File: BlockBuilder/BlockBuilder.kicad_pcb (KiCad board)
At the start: 4 copper layers, 1 x 55.8 mm, 82 parts, among them J1 ARJM11C7-114-BA-EW2, T1 FA2924-AL, U1 W5500, U2 Si3402-B-GMR, U3 VO618A-3X017T, U4 TLV431BCDBZR, Y1 25.000MHz CL=12pF

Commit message: Finish the layout blocks: placement tests pass, docs updated
All nine fragments passed the BlockBuilder placement test on 2026-09-25:
footprints, segments, vias, zones and F.Fab labels arrived, and copper
matched each module board net by net. BlockBuilder keeps the PoE retest.

Per-footprint zone-connection overrides do not travel with a fragment. The
Buck, PowerMux and USBC Host-Setup pages say how to set the power pads to
solid in the host.

The PoE module gets its review-fix record (Layout-Spec section 17) and the new
line-side rule in Host-Setup. TODO.md closes the layout block list and lists
the fab questions and known limits. ARCHITECTURE.md carries the new
placement measurement.

Co-Authored-By: Claude Opus 5.5 (1M context) <noreply@anthropic.com>
Claude-Session: https://claude.ai/code/session_01ErAAfkmF4h3T5yfrw21utF
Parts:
- moved C10 62.9 mm to (44.0, 32.0)
- moved C12 62.9 mm to (44.0, 34.3)
- moved C14 62.9 mm to (38.0, 37.7)
- moved C15 62.9 mm to (60.5, 44.0)
- moved C17 62.9 mm to (44.0, 36.5)
- moved C18 62.9 mm to (49.2, 44.0)
- moved C21 62.9 mm to (49.2, 47.0)
- moved C22 62.9 mm to (53.0, 47.5)
- moved C24 62.9 mm to (35.0, 52.0)
- moved C25 62.9 mm to (47.0, 29.5)
- moved C26 62.9 mm to (47.0, 23.0)
- moved C27 62.9 mm to (44.5, 41.5)
- moved C28 62.9 mm to (54.0, 24.0)
- moved C30 62.9 mm to (36.2, 46.0)
- moved C33 62.9 mm to (44.5, 39.5)
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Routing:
- net /VPOS: track 5.15 -> 8.93 mm
- net GND: track 3.49 -> 7.03 mm, vias 11 -> 55
- net /MDI_RDP: track 23.0 -> 23.8 mm
- net /RCT: track 27.2 -> 27.9 mm
- net /XO: track 11.4 -> 10.8 mm
- net /MDI_RDN: track 19.4 -> 19.9 mm

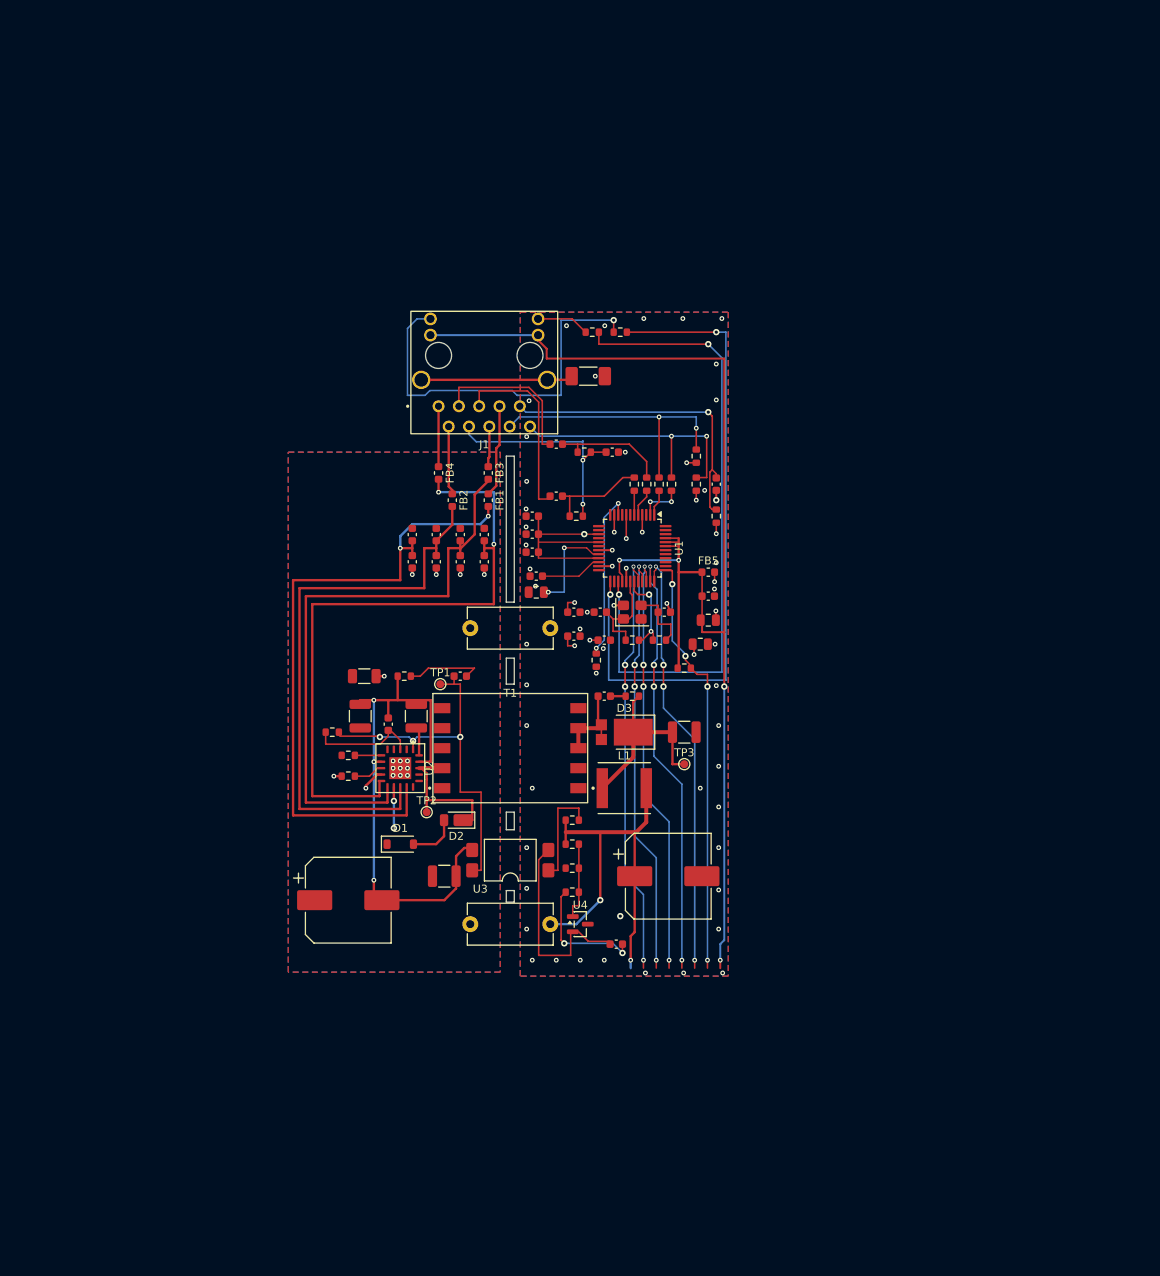
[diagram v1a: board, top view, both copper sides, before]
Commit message: Put the PoE block schematic on one A3 page
The block schematic spanned 296 mm on an A4 landscape page, and 37 of its 82
parts sat above the frame, so a print lost them.

- Two sheets inside one block do not work: KiCad 10.0.6 refuses to save a
  design block with a nested sheet. Tested on a scratch project.
- The sheet is now A3 portrait with every part inside the frame. Net
  membership is identical to before the move, ERC and DRC are unchanged, and
  the fragment's schematic is updated.
- Placed with Place as sheet, the block lands as its own A3 page with its
  title block. The full layout arrives, copper equal net by net.

Place as sheet prefixes every net with the sheet path, so /NAME net class
patterns bind nothing. Every Host-Setup.md now has section 5.3: use */NAME,
which binds the same nets on a flat placement.

BlockBuilder keeps this test.

Co-Authored-By: Claude Opus 5.5 (1M context) <noreply@anthropic.com>
Claude-Session: https://claude.ai/code/session_01ErAAfkmF4h3T5yfrw21utF
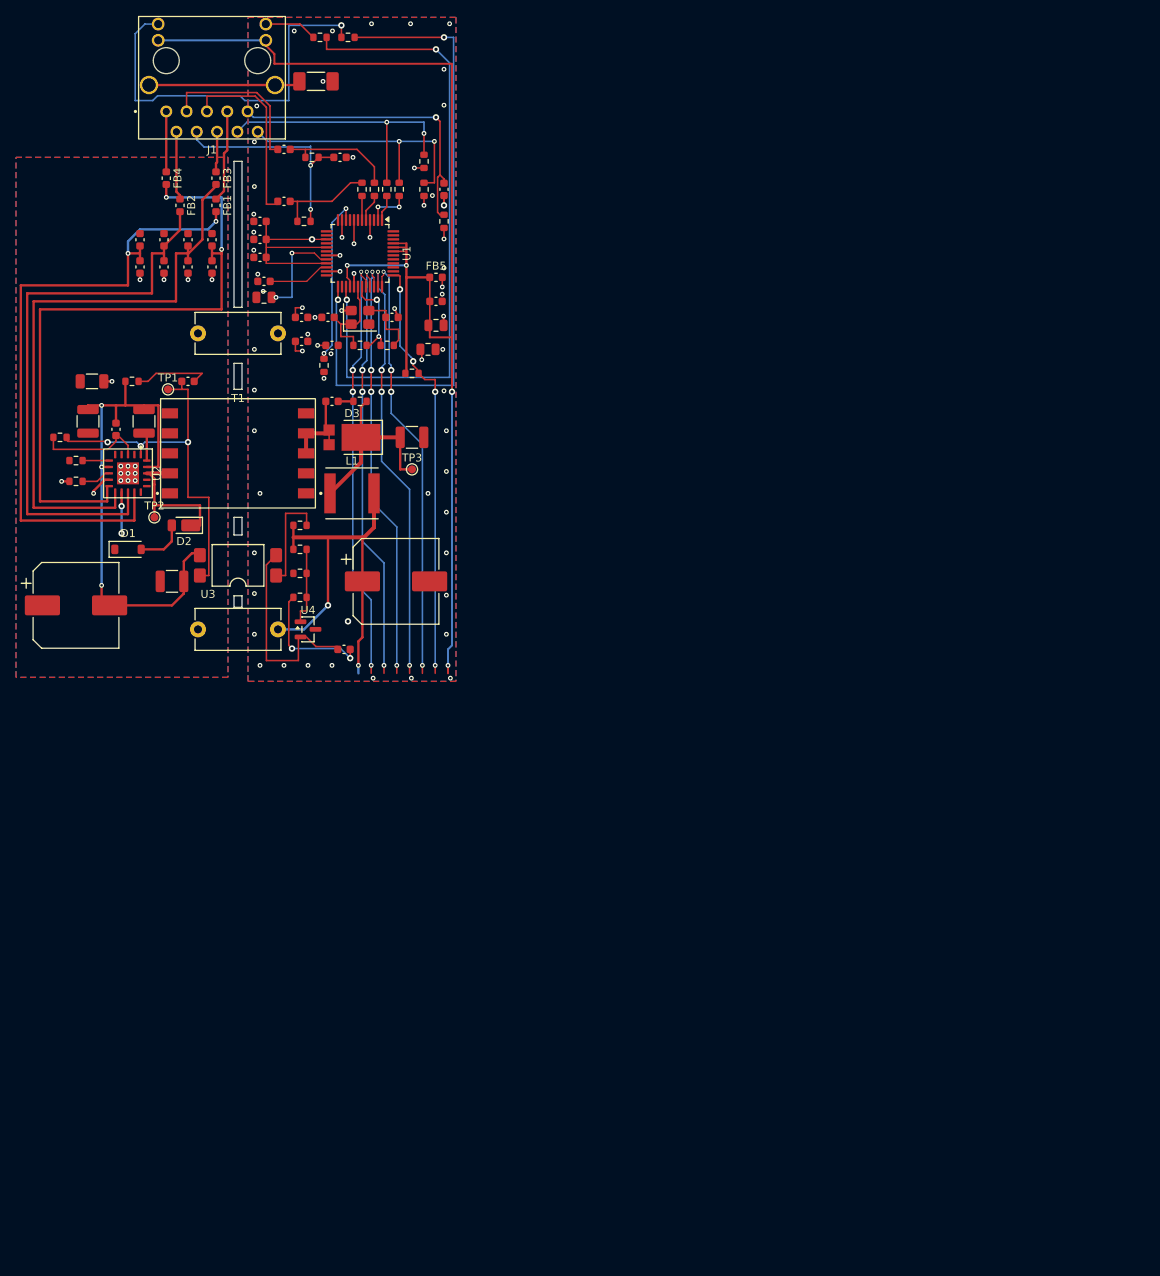
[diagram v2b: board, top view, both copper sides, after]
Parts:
- moved D1 50.2 mm to (-6.54, 36.2)
- moved TP2 50.2 mm to (-3.24, 32.2)
- moved C1 50.2 mm to (-5.04, -2.52)
- moved C10 50.2 mm to (9.96, -4.83)
- moved C12 50.2 mm to (9.96, -2.58)
- moved C13 50.2 mm to (3.96, -2.52)
- moved C14 50.2 mm to (3.96, 0.88)
- moved C15 50.2 mm to (26.5, 7.17)
- moved C16 50.2 mm to (-1.04, 40.2)
- moved C17 50.2 mm to (9.96, -0.33)
- moved C18 50.2 mm to (15.2, 7.17)
- moved C2 50.2 mm to (-5.04, 0.88)
- moved C23 50.2 mm to (31.0, 11.2)
- moved C25 50.2 mm to (13.0, -7.33)
- moved C27 50.2 mm to (10.5, 4.67)
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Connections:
- net /3V3A renamed /PoE-Ethernet-Si3402-W5500/3V3A
- net /ACTLED renamed /PoE-Ethernet-Si3402-W5500/ACTLED
- net /CGND renamed /PoE-Ethernet-Si3402-W5500/CGND
- net /CLAMP_MID renamed /PoE-Ethernet-Si3402-W5500/CLAMP_MID
- net /COMP_PRI renamed /PoE-Ethernet-Si3402-W5500/COMP_PRI
- net /COMP_SEC renamed /PoE-Ethernet-Si3402-W5500/COMP_SEC
- net /CT1_NET renamed /PoE-Ethernet-Si3402-W5500/CT1_NET
- net /CT2_NET renamed /PoE-Ethernet-Si3402-W5500/CT2_NET
- net /EROUT renamed /PoE-Ethernet-Si3402-W5500/EROUT
- net /ETH_CLK renamed /PoE-Ethernet-Si3402-W5500/ETH_CLK
- net /ETH_CS renamed /PoE-Ethernet-Si3402-W5500/ETH_CS
- net /ETH_INT renamed /PoE-Ethernet-Si3402-W5500/ETH_INT
- net /ETH_MISO renamed /PoE-Ethernet-Si3402-W5500/ETH_MISO
- net /ETH_MOSI renamed /PoE-Ethernet-Si3402-W5500/ETH_MOSI
- net /ETH_RST renamed /PoE-Ethernet-Si3402-W5500/ETH_RST
- net /EXRES1 renamed /PoE-Ethernet-Si3402-W5500/EXRES1
- net /FB_REF renamed /PoE-Ethernet-Si3402-W5500/FB_REF
- net /LED_ACT_K renamed /PoE-Ethernet-Si3402-W5500/LED_ACT_K
- net /LED_LINK_K renamed /PoE-Ethernet-Si3402-W5500/LED_LINK_K
- net /LINKLED renamed /PoE-Ethernet-Si3402-W5500/LINKLED
- net /MDI_RDN renamed /PoE-Ethernet-Si3402-W5500/MDI_RDN
- net /MDI_RDP renamed /PoE-Ethernet-Si3402-W5500/MDI_RDP
- net /OPTO_LED_A renamed /PoE-Ethernet-Si3402-W5500/OPTO_LED_A
- net /POE_5V renamed /PoE-Ethernet-Si3402-W5500/POE_5V
- net /POE_VC1N renamed /PoE-Ethernet-Si3402-W5500/POE_VC1N
- net /POE_VC1P renamed /PoE-Ethernet-Si3402-W5500/POE_VC1P
- net /POE_VC2N renamed /PoE-Ethernet-Si3402-W5500/POE_VC2N
- net /POE_VC2P renamed /PoE-Ethernet-Si3402-W5500/POE_VC2P
- net /RCL renamed /PoE-Ethernet-Si3402-W5500/RCL
- net /RCT renamed /PoE-Ethernet-Si3402-W5500/RCT
- net /RDET renamed /PoE-Ethernet-Si3402-W5500/RDET
- net /RXN_CHIP renamed /PoE-Ethernet-Si3402-W5500/RXN_CHIP
- net /RXN_T renamed /PoE-Ethernet-Si3402-W5500/RXN_T
- net /RXP_CHIP renamed /PoE-Ethernet-Si3402-W5500/RXP_CHIP
- net /RXP_T renamed /PoE-Ethernet-Si3402-W5500/RXP_T
- net /SEC_A renamed /PoE-Ethernet-Si3402-W5500/SEC_A
- net /SNUB_MID renamed /PoE-Ethernet-Si3402-W5500/SNUB_MID
- net /SP1_NET renamed /PoE-Ethernet-Si3402-W5500/SP1_NET
- net /SP2_NET renamed /PoE-Ethernet-Si3402-W5500/SP2_NET
- net /SWO renamed /PoE-Ethernet-Si3402-W5500/SWO
- net /TCT renamed /PoE-Ethernet-Si3402-W5500/TCT
- net /TLV_K renamed /PoE-Ethernet-Si3402-W5500/TLV_K
- net /TOCAP renamed /PoE-Ethernet-Si3402-W5500/TOCAP
- net /TXN_CHIP renamed /PoE-Ethernet-Si3402-W5500/TXN_CHIP
- net /TXN_MDI renamed /PoE-Ethernet-Si3402-W5500/TXN_MDI
- net /TXP_CHIP renamed /PoE-Ethernet-Si3402-W5500/TXP_CHIP
- net /TXP_MDI renamed /PoE-Ethernet-Si3402-W5500/TXP_MDI
- net /V1V2O renamed /PoE-Ethernet-Si3402-W5500/V1V2O
- net /VDD_PRI renamed /PoE-Ethernet-Si3402-W5500/VDD_PRI
- net /VNEG renamed /PoE-Ethernet-Si3402-W5500/VNEG
- net /VOUT_RAW renamed /PoE-Ethernet-Si3402-W5500/VOUT_RAW
- net /VPOS renamed /PoE-Ethernet-Si3402-W5500/VPOS
- net /VSS_PRI renamed /PoE-Ethernet-Si3402-W5500/VSS_PRI
- net /XI renamed /PoE-Ethernet-Si3402-W5500/XI
- net /XO renamed /PoE-Ethernet-Si3402-W5500/XO
- net /XTAL_B renamed /PoE-Ethernet-Si3402-W5500/XTAL_B
